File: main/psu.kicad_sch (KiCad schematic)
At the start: 27 parts, among them U102 LMR51430, U302 LDK130M33R, U303 LM317_SOT-223

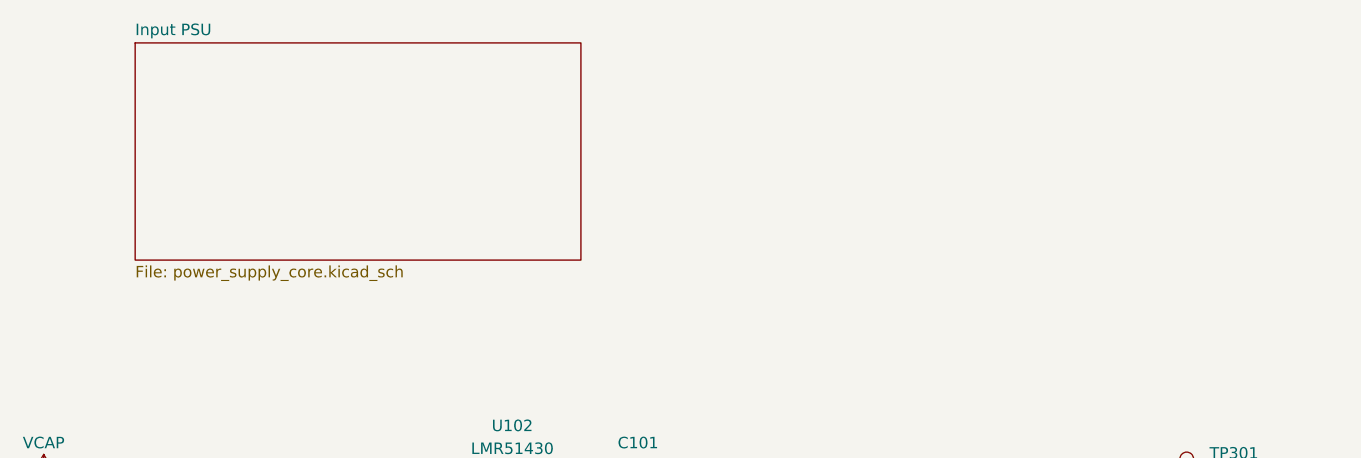
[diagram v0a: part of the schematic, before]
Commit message: Start design of new PSU
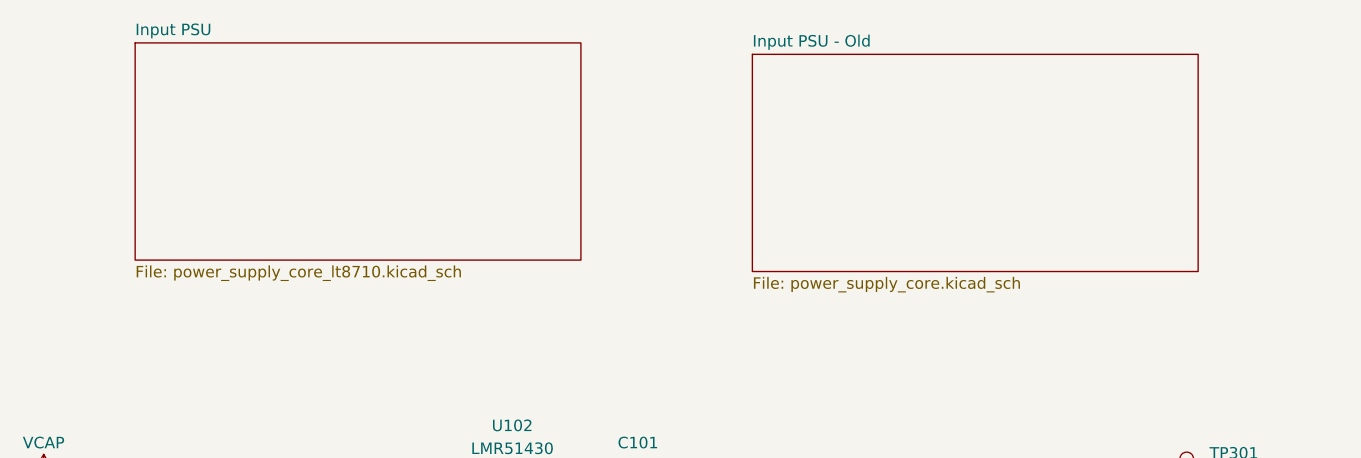
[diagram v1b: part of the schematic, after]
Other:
- added sheet Input PSU - Old (power_supply_core.kicad_sch)
- sheet Input PSU: file power_supply_core.kicad_sch -> power_supply_core_lt8710.kicad_sch

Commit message: [PSU] Compute values for LT8710 PSU
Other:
- company: (none) -> Julien FAUCHER
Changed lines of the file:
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@@
 (kicad_sch (version 20230819) (generator eeschema)
   (paper "A4")
+  (title_block
+    (date "2023-04-05")
+    (rev "0.1")
+    (company "Julien FAUCHER")
+    (comment 1 "Defis solaires 2024")
+  )
   (junction (at 71.12 99.06) (diameter 0) (color 0 0 0 0)
   )

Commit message: PSU should be OK
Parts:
- renumbered C101 to C401, C102 to C402, C102 to C403, C310 to C404, C311 to C405, C102 to C406, C103 to C407, C309 to C408, C102 to C409, C308 to C410, C306 to C411, C305 to C412, C307 to C413, D201 to D401, L101 to L401, R102 to R401, R307 to R402, R101 to R403, R102 to R404, R103 to R405, R305 to R406, R306 to R407, TP302 to TP401, TP301 to TP402, U102 to U401, U302 to U402, U303 to U403
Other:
- removed sheet Input PSU - Old
- sheet Input PSU ports: added V_{CTRL}, V_{IN}, V_{OUT}; removed none

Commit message: Progresses
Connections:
- net PGND: no longer C404.2, C405.2, C408.2, C409.2, U402.2 (GND)
- net VCAP renamed V_{CAP}
- new net GNDD: C404.2, C405.2, C408.2, C409.2, U402.2 (GND)
- no-connect marks 0 -> 1
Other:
- note added: "Feedback resistor for compatibility with LDK130 witout fixed output or other part."
- note added: "To a supercap bank"
- moved on the sheet: C401, C402, C403, C404, C405, C406, C407, C408, C409, C410, C411, C412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

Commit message: Update schematics
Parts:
- added JP401: DRIVE VSEL, symbol Jumper:Jumper_3_Bridged12
- C410, C411, C412, C413, D401, R406, R407, U403: now not fitted; now left out of the parts list
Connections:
- net +12V: now also JP401.3 (B)
- net V_{CAP}: now also JP401.1 (A)
- new net V_{DRIVE}: JP401.2 (C)
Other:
- note added: "Aux HV PSU Should not be required as driven components would allow VCAP as a proper PSU."
- note added: "V_{CAP}"

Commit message: Some work
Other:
- added sheet Battery chagrer (battery_charger.kicad_sch)
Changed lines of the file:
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@@
 (kicad_sch
-	(version 20231120)
+	(version 20240101)
 	(generator "eeschema")
-	(generator_version "8.0")
+	(generator_version "8.99")
 	(paper "A4")
 	(title_block
@@
 				)
 			)
+		)
+	)
+	(sheet
+		(at 134.62 29.21)
+		(size 38.1 20.32)
+		(fields_autoplaced yes)
+		(stroke
+			(width 0.1524)
+			(type solid)
+		)
+		(fill
+			(color 0 0 0 0.0000)
+		)
+		(property "Sheetname" "Battery chagrer"
+			(at 134.62 28.4984 0)
+			(effects
+				(font
+					(size 1.27 1.27)
+				)
+				(justify left bottom)
+			)
+		)
+		(property "Sheetfile" "battery_charger.kicad_sch"
+			(at 134.62 50.1146 0)
+			(effects
+				(font
+					(size 1.27 1.27)
+				)
+				(justify left top)
+			)
+		)
+		(instances
+			(project "dsv4"
+				(path "/c07e9297-fde8-4755-803e-d05072cd6096/164e5be8-13e0-4d66-ab9d-977f2147e774"
+					(page "16")
+				)
+			)

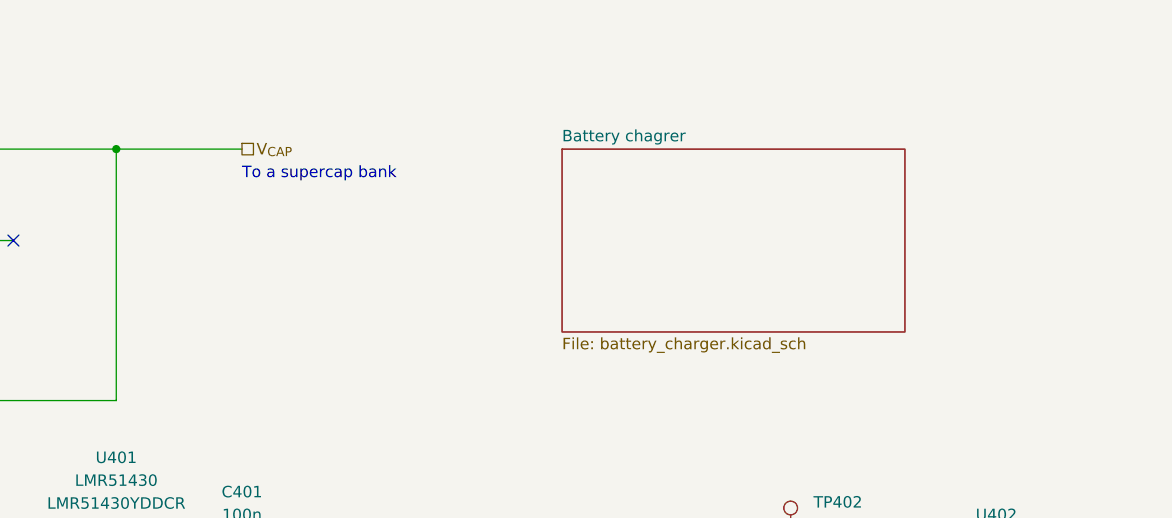
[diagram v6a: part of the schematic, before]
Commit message: Finalize schema for bat charger
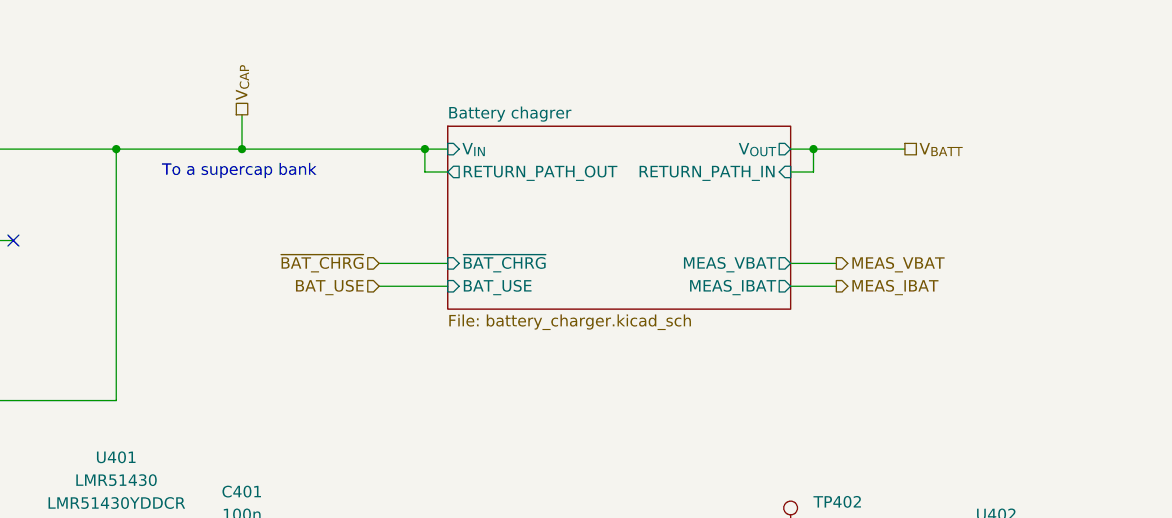
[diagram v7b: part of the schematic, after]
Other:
- sheet Battery chagrer ports: added BAT_USE, MEAS_IBAT, MEAS_VBAT, RETURN_PATH_IN, RETURN_PATH_OUT, V_{IN}, V_{OUT}, ~{BAT_CHRG}; removed none

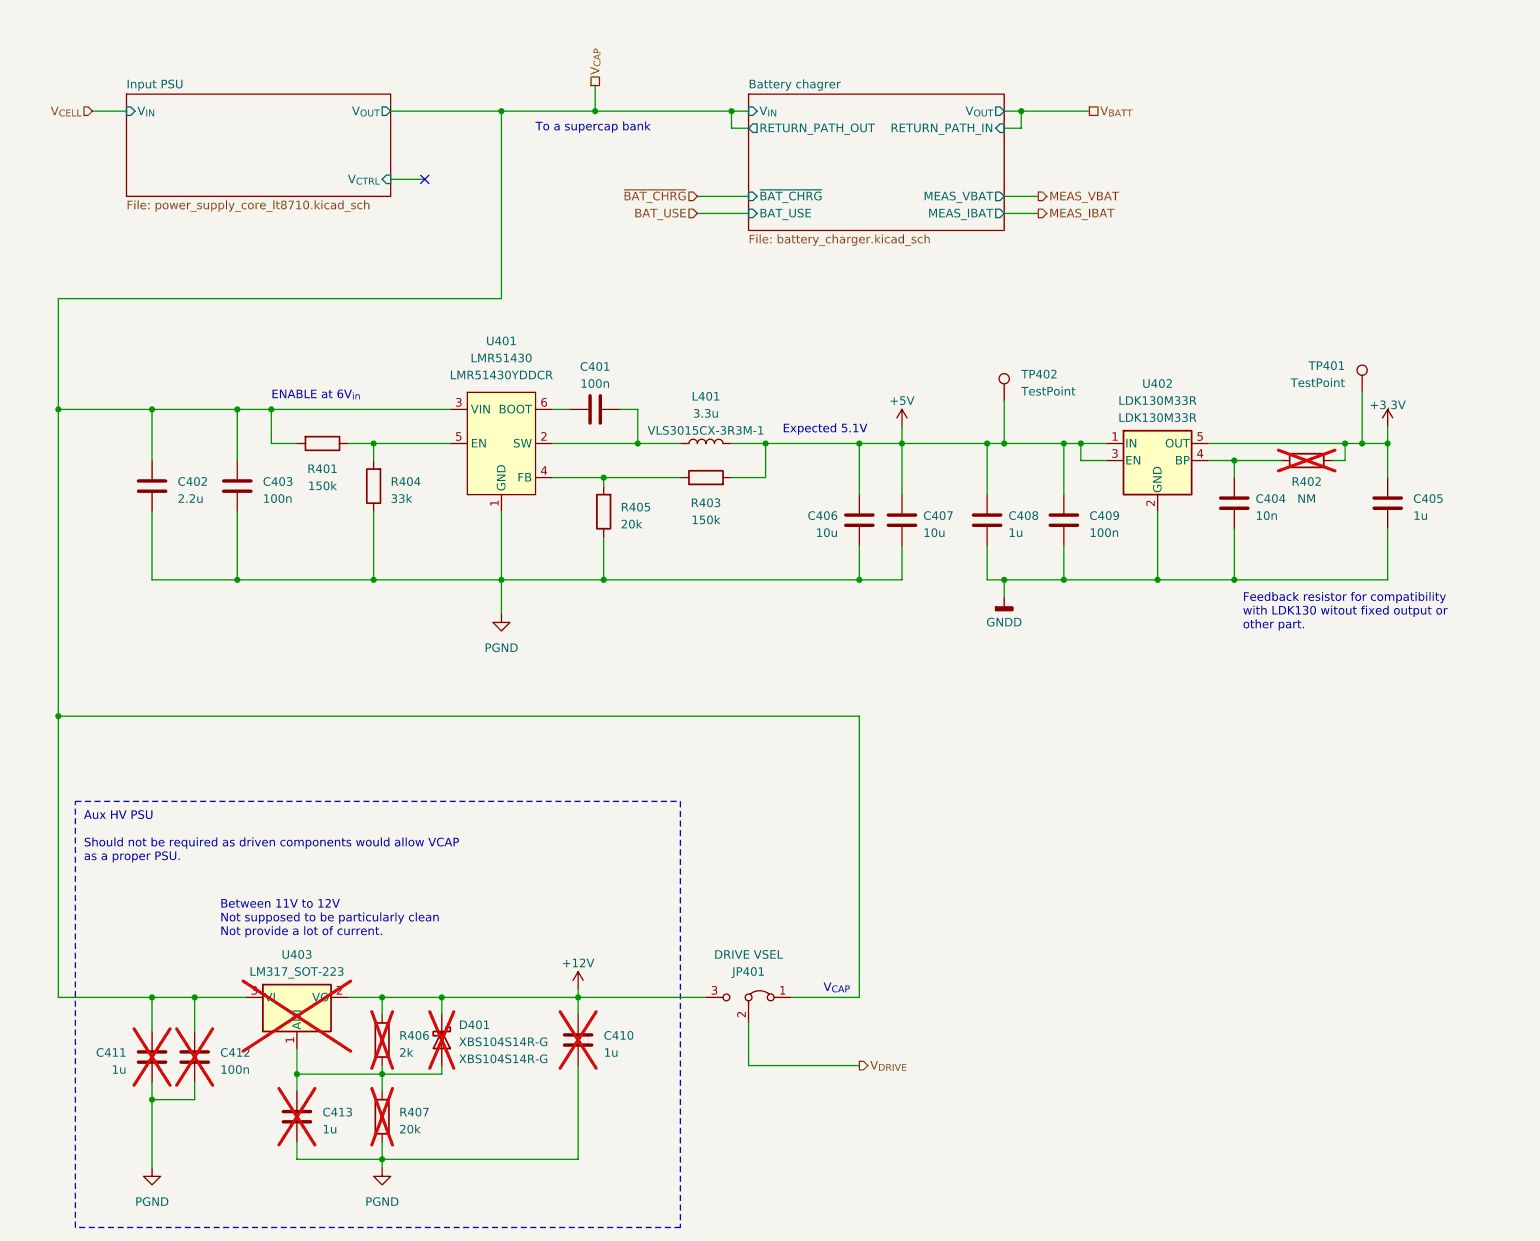
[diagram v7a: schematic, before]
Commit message: Finalize sch and start component mapping
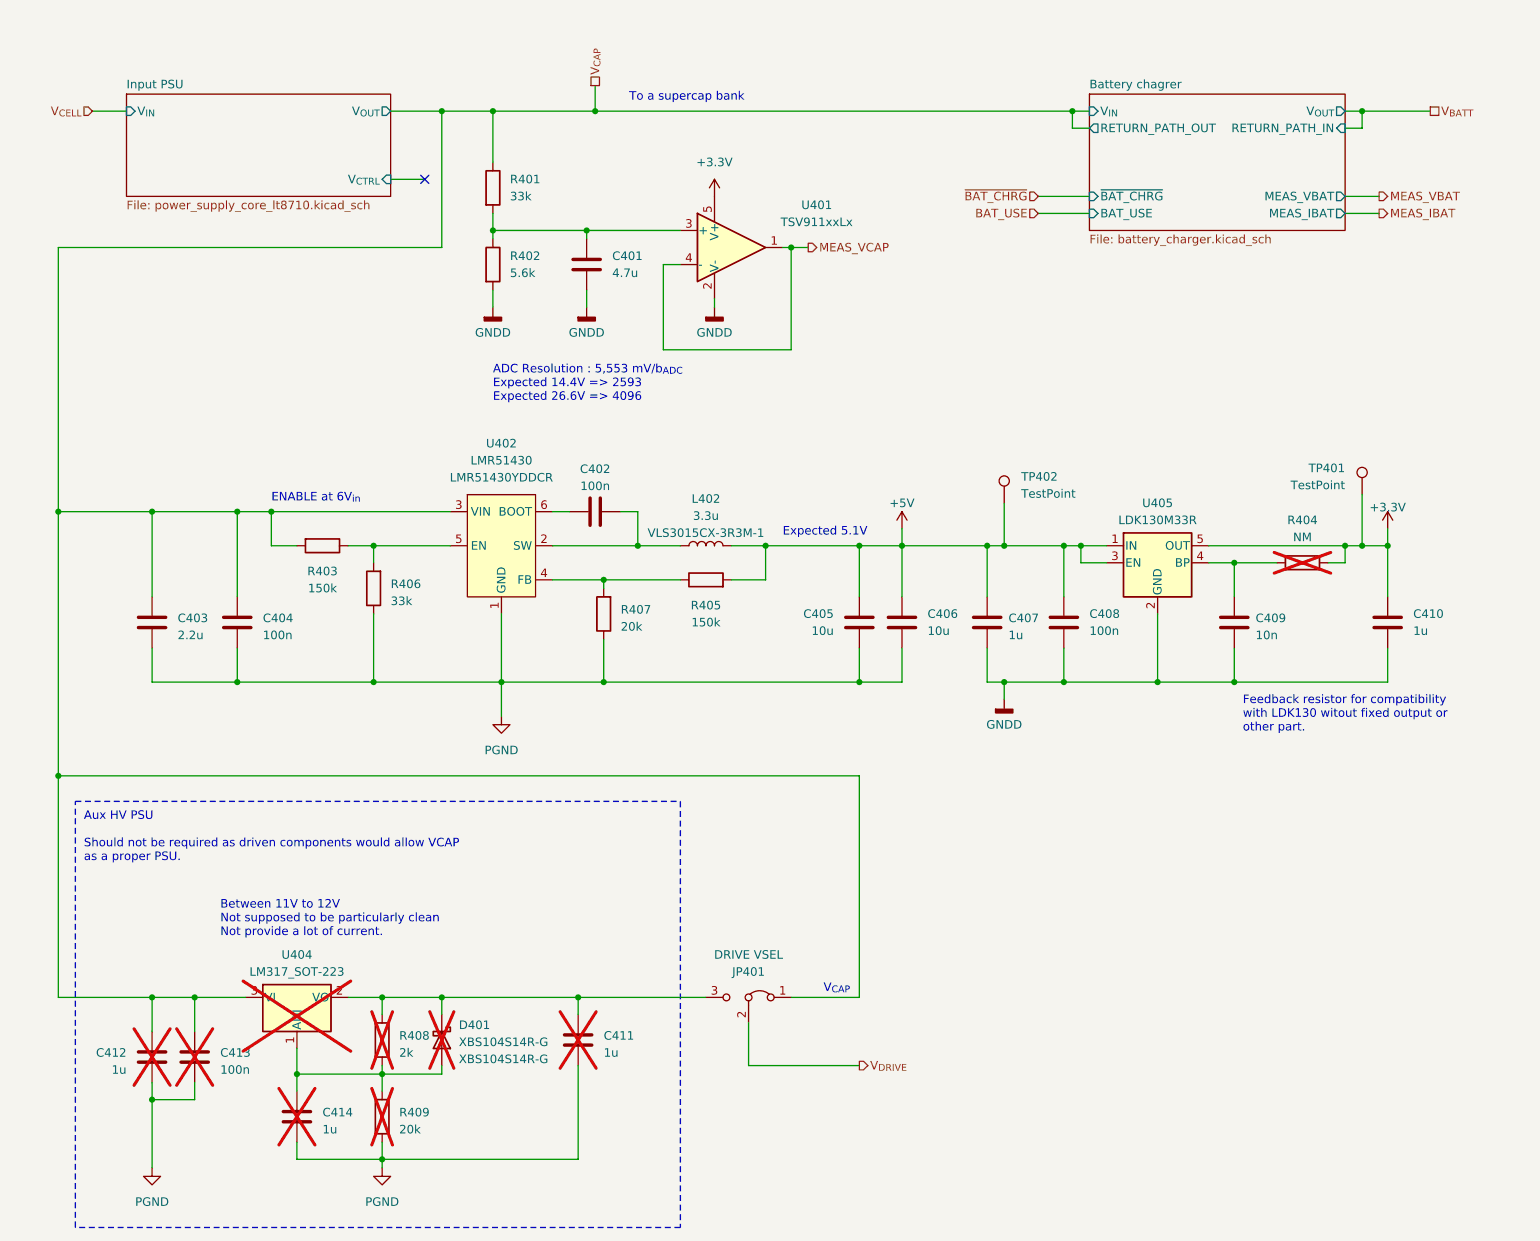
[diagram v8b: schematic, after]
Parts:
- removed C407: 10u, Capacitor_SMD:C_0805_2012Metric, symbol Device:C
- removed C409: 100n, Capacitor_SMD:C_0805_2012Metric, symbol Device:C
- removed L401: 3.3u, power_supply:VLS3015CX, symbol Device:L
- removed U402: LDK130M33R, Package_TO_SOT_SMD:SOT-23-5, symbol Regulator_Linear:LDK130-33_SOT23_SOT353
- added C401: 4.7u, Capacitor_SMD:C_0805_2012Metric, symbol Device:C
- added C408: 100n, Capacitor_SMD:C_0805_2012Metric, symbol Device:C
- added C410: 1u, Capacitor_SMD:C_0805_2012Metric, symbol Device:C
- added L402: 3.3u, power_supply:VLS3015CX, symbol Device:L
- added R401: 33k, Resistor_SMD:R_0805_2012Metric, symbol Device:R
- added R404: NM, Resistor_SMD:R_0805_2012Metric, symbol Device:R
- added U401: TSV911xxLx, Package_TO_SOT_SMD:SOT-23-5, symbol Amplifier_Operational:TSV911xxLx
- added U405: LDK130M33R, Package_TO_SOT_SMD:SOT-23-5, symbol Regulator_Linear:LDK130-33_SOT23_SOT353
- C405: value 1u -> 10u
- C411: renamed from C410; footprint (none) -> Capacitor_SMD:C_0805_2012Metric
- C412: renamed from C411; footprint (none) -> Capacitor_SMD:C_0805_2012Metric
- C413: renamed from C412; footprint (none) -> Capacitor_SMD:C_0805_2012Metric
- C414: renamed from C413; footprint (none) -> Capacitor_SMD:C_0805_2012Metric
- R402: value NM -> 5.6k; now fitted; now in the parts list
- R408: renamed from R406; footprint (none) -> Resistor_SMD:R_0805_2012Metric
- R409: renamed from R407; footprint (none) -> Resistor_SMD:R_0805_2012Metric
- TP401, TP402: now in the parts list
- renumbered C401 to C402, C402 to C403, C403 to C404, C408 to C407, C404 to C409, R401 to R403, R403 to R405, R404 to R406, R405 to R407, U401 to U402, U403 to U404
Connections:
- net +3.3V: now also C410.1, R404.1, U401.5 (V+), U405.5 (OUT); no longer C405.1, R402.2
- net +5V: now also C405.1, C408.1, L402.2, U405.1 (IN), U405.3 (EN)
- net GNDD: now also R402.2, C401.2, C408.2, C410.2, U401.2 (V-), U405.2 (GND); no longer C405.2
- net PGND: now also C405.2
- net V_{CAP}: now also R401.1
- net at R402.1: now also C401.1, R401.2, U401.3 (+); no longer C409.1
- net at C402.2, U402.2 (SW): now also L402.1
- net +12V: no longer names the net of C411.1, D401.1 (K), JP401.3 (B), R408.1, U404.2 (VO)
- new net: C409.1, R404.2, U405.4 (BP)
- new net MEAS_VCAP: U401.1, U401.4 (-)
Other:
- note added: "ADC Resolution : 5,553 mV/b_{ADC} Expected 14.4V => 2593 Expected 26.6V => 4096"
- moved on the sheet: C402, C403, C404, C407, C409, R403, R405, R406, R407, TP401, TP402, U402
